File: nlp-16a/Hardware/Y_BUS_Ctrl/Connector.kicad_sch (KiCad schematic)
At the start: 62 parts, among them J1 Conn_02x20_Odd_Even, J2 Conn_02x20_Odd_Even, J3 Conn_02x10_Odd_Even, J4 Conn_02x10_Counter_Clockwise, J5 Screw_Terminal_01x02

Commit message: Y-BUS制御完成
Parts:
- added R33: 22, Resistor_SMD:R_0603_1608Metric_Pad0.98x0.95mm_HandSolder, symbol Device:R
- added U43: CD74HC00, Package_DIP:DIP-14_W7.62mm, symbol CD74HCXX:CD74HC00
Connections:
- net GND: now also U43.7 (GND), U43.7 (GND), U43.7 (GND), U43.7 (GND)
- net VCC: now also U43.14 (VCC), U43.14 (VCC), U43.14 (VCC), U43.14 (VCC)
- net phi1: now also U43.1, U43.2; no longer J1.36 (Pin_36)
- new net: U43.10, U43.12, U43.13, U43.3, U43.4, U43.5, U43.9
- new net: R33.1, U43.6
- new net phi1_Reg1: U43.11
- new net phi1_Reg2: U43.8
- new net phi1_bus: J1.36 (Pin_36), R33.2
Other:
- moved on the sheet: J3, J4

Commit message: Y BUS制御 更新
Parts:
- added C22, C23: C, Capacitor_THT:C_Disc_D7.5mm_W2.5mm_P5.00mm, symbol Device:C
- added D33, D34, D35: LED, LED_THT:LED_D3.0mm, symbol Device:LED
- added R34: 22, Resistor_SMD:R_0603_1608Metric_Pad0.98x0.95mm_HandSolder, symbol Device:R
- added R35, R36, R37: R, Resistor_SMD:R_0603_1608Metric_Pad0.98x0.95mm_HandSolder, symbol Device:R
- added U44: CD74HC00, Package_DIP:DIP-14_W7.62mm, symbol CD74HCXX:CD74HC00
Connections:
- net GND: now also C22.1, C23.1, R35.2, R36.2, R37.2, U44.7 (GND), U44.7 (GND), U44.7 (GND), U44.7 (GND)
- net VCC: now also C22.2, C23.2, D35.2 (A), U44.14 (VCC), U44.14 (VCC), U44.14 (VCC), U44.14 (VCC)
- net phi1_Reg2: now also D34.2 (A)
- net phi2: now also U44.1, U44.2; no longer J1.34 (Pin_34), J3.1 (Pin_1)
- new net: R34.1, U44.11
- new net: U44.10, U44.12, U44.13, U44.3, U44.4, U44.5, U44.9
- new net: D33.1 (K), R35.1
- new net: D34.1 (K), R36.1
- new net: D35.1 (K), R37.1
- new net: D33.2 (A), U44.6
- new net phi2_Acc: J3.1 (Pin_1), U44.8
- new net phi2_bus: J1.34 (Pin_34), R34.2
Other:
- note added: "ALU Ctrl Conn"
- note added: "Acc Conn"
- note added: "Clock"
- note added: "Power"
- note added: "Y BUS Conn"
- note added: "Y BUS Ctrl Conn"
- moved on the sheet: C1, C10, C11, C12, C13, C14, C15, C16, C17, C18, C19, C2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

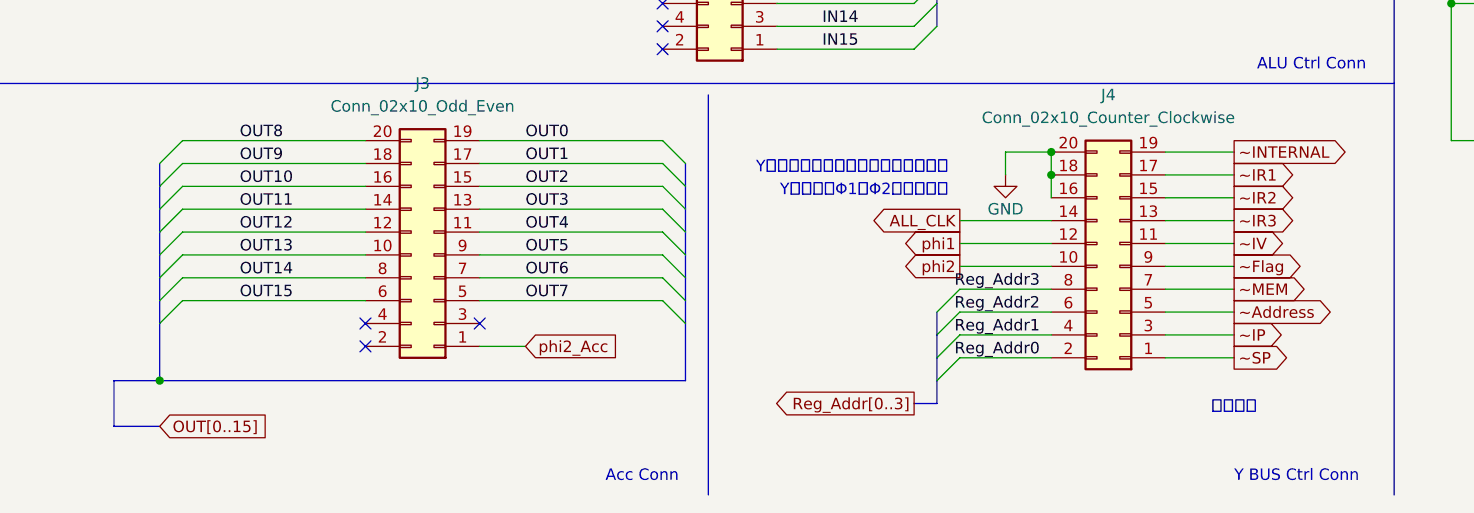
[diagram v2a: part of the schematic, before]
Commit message: Y BUS制御 IV -> Acc ENの修正
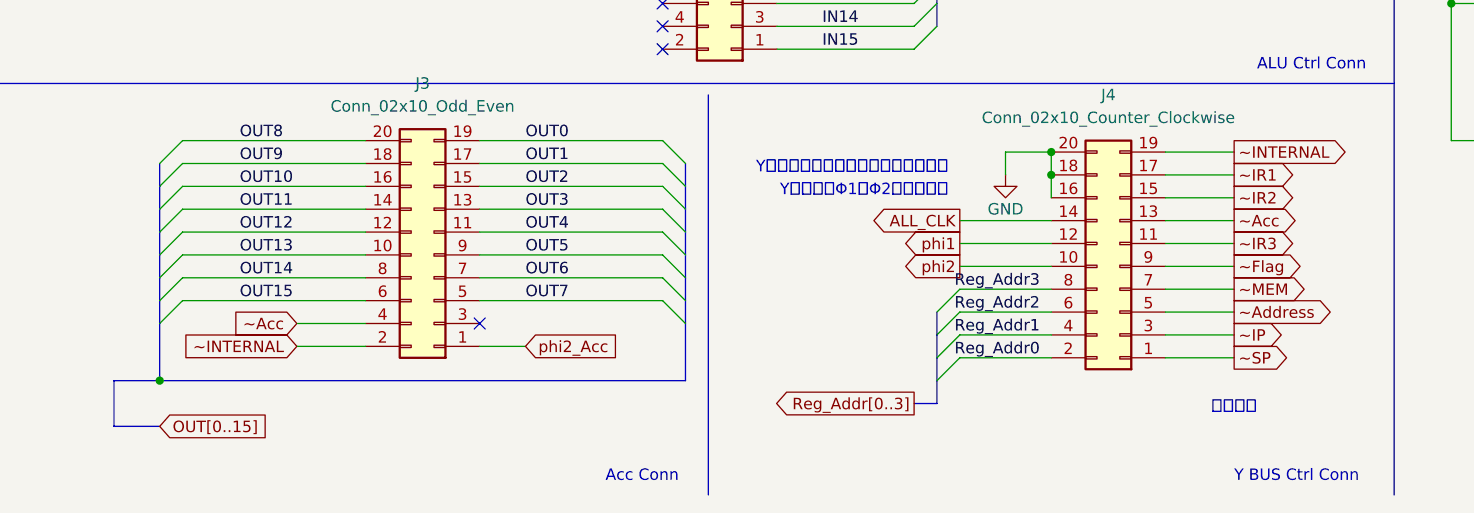
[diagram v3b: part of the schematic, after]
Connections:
- net ~IV is gone; now on net ~IR3: J4.11 (Pin_11)
- net ~INTERNAL: now also J3.2 (Pin_2)
- net ~IR3: no longer J4.13 (Pin_13)
- net ~Acc: now reaches J3.4 (Pin_4)
- net ~Acc: now also J4.13 (Pin_13)
- no-connect marks 23 -> 21
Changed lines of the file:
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@@
   (no_connect (at 87.63 144.78))
   (no_connect (at 67.31 177.8))
-  (no_connect (at 54.61 177.8))
   (no_connect (at 87.63 116.84))
-  (no_connect (at 54.61 180.34))
   (no_connect (at 87.63 142.24))
   (no_connect (at 87.63 134.62))
@@
     (stroke (width 0) (type default) (color 0 0 0 0))
   )
+  (wire (pts (xy 46.99 180.34) (xy 54.61 180.34))
+    (stroke (width 0) (type default) (color 0 0 0 0))
+  )
   (bus (pts (xy 135.89 68.58) (xy 135.89 71.12))
     (stroke (width 0) (type default) (color 0 0 0 0))
@@
   )
   (wire (pts (xy 182.88 134.62) (xy 191.77 134.62))
+    (stroke (width 0) (type default) (color 0 0 0 0))
+  )
+  (wire (pts (xy 46.99 177.8) (xy 54.61 177.8))
     (stroke (width 0) (type default) (color 0 0 0 0))
   )
@@
     )
   )
+  (global_label "~Acc" (shape input) (at 46.99 177.8 180) (fields_autoplaced)
+    (effects (font (size 1.27 1.27)) (justify right))
+    (property "Intersheet References" "${INTERSHEET_REFS}" (id 0) (at 40.404 177.7206 0)
+      (effects (font (size 1.27 1.27)) (justify right) hide)
+    )
+  )
   (global_label "~Address" (shape output) (at 151.13 176.53 0) (fields_autoplaced)
     (effects (font (size 1.27 1.27)) (justify left))
@@
     )
   )
-  (global_label "~IV" (shape output) (at 151.13 168.91 0) (fields_autoplaced)
+  (global_label "~Acc" (shape output) (at 151.13 166.37 0) (fields_autoplaced)
     (effects (font (size 1.27 1.27)) (justify left))
-    (property "Intersheet References" "${INTERSHEET_REFS}" (id 0) (at 156.1436 168.8306 0)
+    (property "Intersheet References" "${INTERSHEET_REFS}" (id 0) (at 157.716 166.2906 0)
       (effects (font (size 1.27 1.27)) (justify left) hide)
     )
@@
     )
   )
-  (global_label "~IR3" (shape output) (at 151.13 166.37 0) (fields_autoplaced)
+  (global_label "~INTERNAL" (shape input) (at 46.99 180.34 180) (fields_autoplaced)
+    (effects (font (size 1.27 1.27)) (justify right))
+    (property "Intersheet References" "${INTERSHEET_REFS}" (id 0) (at 34.9007 180.2606 0)
+      (effects (font (size 1.27 1.27)) (justify right) hide)
+    )
+  )
+  (global_label "~IR3" (shape output) (at 151.13 168.91 0) (fields_autoplaced)
     (effects (font (size 1.27 1.27)) (justify left))
-    (property "Intersheet References" "${INTERSHEET_REFS}" (id 0) (at 157.5345 166.2906 0)
+    (property "Intersheet References" "${INTERSHEET_REFS}" (id 0) (at 157.5345 168.8306 0)
       (effects (font (size 1.27 1.27)) (justify left) hide)
     )

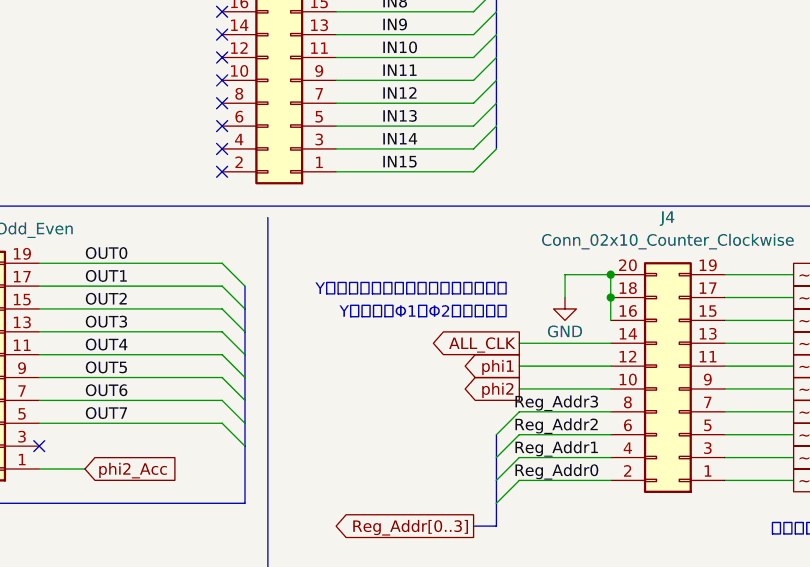
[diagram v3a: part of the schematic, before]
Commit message: Y BUS制御リセット端子にプルアップ追加
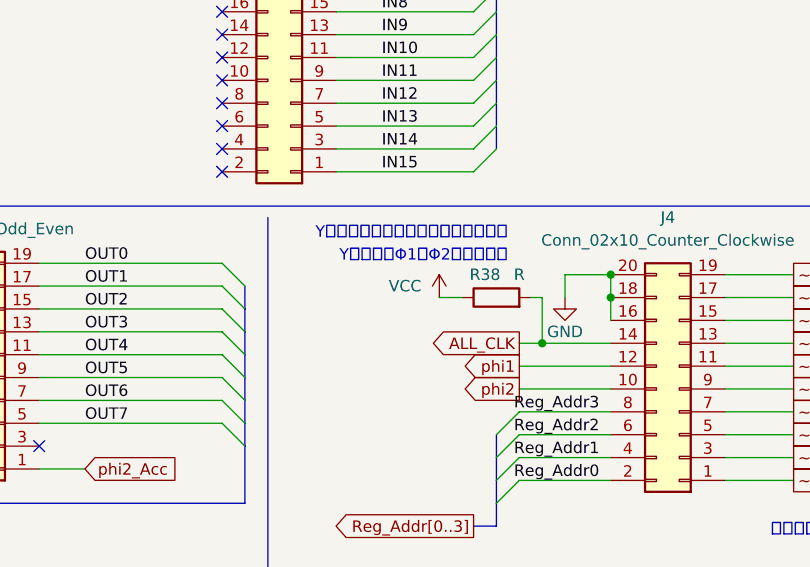
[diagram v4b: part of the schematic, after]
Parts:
- added R38: R, Resistor_SMD:R_0603_1608Metric_Pad0.98x0.95mm_HandSolder, symbol Device:R
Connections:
- net ALL_CLK: now also R38.2
- net VCC: now also R38.1
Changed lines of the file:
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@@
   (junction (at 191.77 157.48) (diameter 0) (color 0 0 0 0)
+  )
+  (junction (at 123.19 166.37) (diameter 0) (color 0 0 0 0)
   )
   (junction (at 218.44 134.62) (diameter 0) (color 0 0 0 0)
@@
     (stroke (width 0) (type default) (color 0 0 0 0))
   )
+  (wire (pts (xy 123.19 161.29) (xy 123.19 166.37))
+    (stroke (width 0) (type default) (color 0 0 0 0))
+  )
   (wire (pts (xy 115.57 134.62) (xy 100.33 134.62))
     (stroke (width 0) (type default) (color 0 0 0 0))
@@
     (stroke (width 0) (type default) (color 0 0 0 0))
   )
+  (wire (pts (xy 111.76 161.29) (xy 114.3 161.29))
+    (stroke (width 0) (type default) (color 0 0 0 0))
+  )
   (wire (pts (xy 191.77 149.86) (xy 182.88 149.86))
     (stroke (width 0) (type default) (color 0 0 0 0))
@@
     (stroke (width 0) (type default) (color 0 0 0 0))
   )
+  (wire (pts (xy 121.92 161.29) (xy 123.19 161.29))
+    (stroke (width 0) (type default) (color 0 0 0 0))
+  )
   (wire (pts (xy 67.31 175.26) (xy 87.63 175.26))
     (stroke (width 0) (type default) (color 0 0 0 0))
@@
     (stroke (width 0) (type default) (color 0 0 0 0))
   )
+  (wire (pts (xy 123.19 166.37) (xy 130.81 166.37))
+    (stroke (width 0) (type default) (color 0 0 0 0))
+  )
   (bus (pts (xy 45.72 53.34) (xy 45.72 55.88))
     (stroke (width 0) (type default) (color 0 0 0 0))
@@
     (stroke (width 0) (type default) (color 0 0 0 0))
   )
-  (wire (pts (xy 120.65 166.37) (xy 130.81 166.37))
+  (wire (pts (xy 120.65 166.37) (xy 123.19 166.37))
     (stroke (width 0) (type default) (color 0 0 0 0))
   )
@@
     (effects (font (size 1.27 1.27)) (justify left bottom))
   )
-  (text "YバスではΦ1，Φ2で使用する" (at 119.38 163.83 180)
+  (text "YバスではΦ1，Φ2で使用する" (at 119.38 157.48 180)
     (effects (font (size 1.27 1.27)) (justify right bottom))
   )
@@
     (effects (font (size 1.27 1.27)) (justify left bottom))
   )
-  (text "Yバスでは全レジスタ指定で使用する" (at 119.38 161.29 180)
+  (text "Yバスでは全レジスタ指定で使用する" (at 119.38 154.94 180)
     (effects (font (size 1.27 1.27)) (justify right bottom))
   )
@@
     (pin "2")
   )
+  (symbol (lib_id "Device:R") (at 118.11 161.29 90) (unit 1)
+    (in_bom yes) (on_board yes)
+    (property "Reference" "R38" (id 0) (at 116.84 158.75 90))
+    (property "Value" "R" (id 1) (at 120.65 158.75 90))
+    (property "Footprint" "Resistor_SMD:R_0603_1608Metric_Pad0.98x0.95mm_HandSolder" (id 2) (at 118.11 163.068 90)
+      (effects (font (size 1.27 1.27)) hide)
+    )
+    (property "Datasheet" "~" (id 3) (at 118.11 161.29 0)
+      (effects (font (size 1.27 1.27)) hide)
+    )
+    (pin "1")
+    (pin "2")
+  )
   (symbol (lib_id "Device:C") (at 254 138.43 0) (unit 1)
     (in_bom yes) (on_board yes) (fields_autoplaced)
@@
     (pin "2")
   )
+  (symbol (lib_id "power:VCC") (at 111.76 161.29 0) (mirror y) (unit 1)
+    (in_bom yes) (on_board yes)
+    (property "Reference" "#PWR026" (id 0) (at 111.76 165.1 0)
+      (effects (font (size 1.27 1.27)) hide)
+    )
+    (property "Value" "VCC" (id 1) (at 107.95 160.02 0))
+    (property "Footprint" "" (id 2) (at 111.76 161.29 0)
+      (effects (font (size 1.27 1.27)) hide)
+    )
+    (property "Datasheet" "" (id 3) (at 111.76 161.29 0)
+      (effects (font (size 1.27 1.27)) hide)
+    )
+    (pin "1")
+  )
   (symbol (lib_id "Device:R") (at 109.22 45.72 90) (unit 1)
